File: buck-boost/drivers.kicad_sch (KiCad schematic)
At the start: 30 parts, among them Q7 Q_NPN_BEC, Q8 Q_NPN_BEC, Q9 Q_NPN_BEC, U4 TBA1-1212E, U5 TBA1-1212E

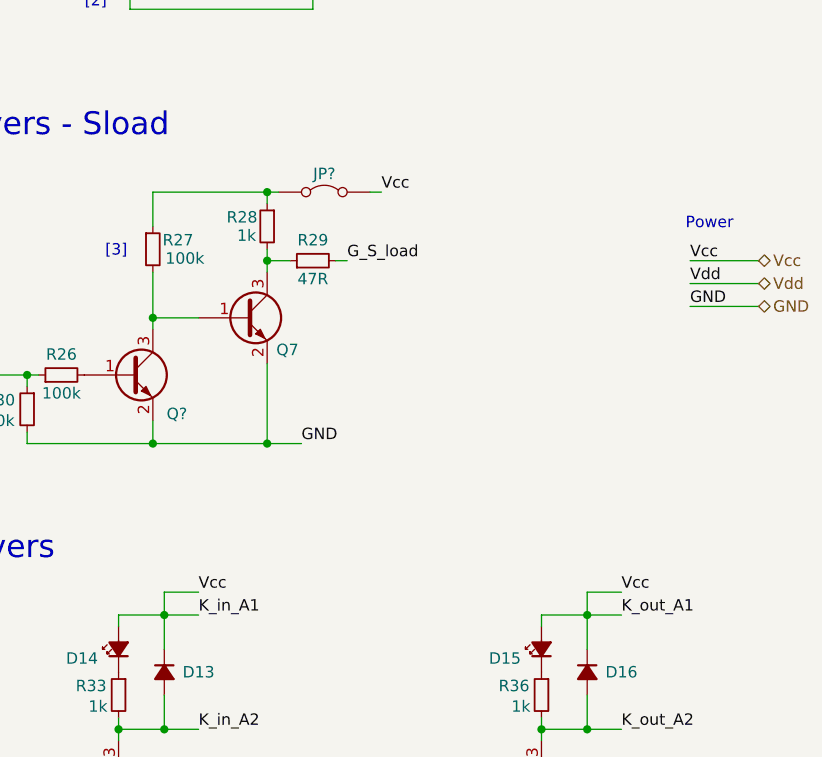
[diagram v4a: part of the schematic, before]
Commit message: The changes indicated in the text document Review. 05.11.2024 were implemented. Missing footprints were added
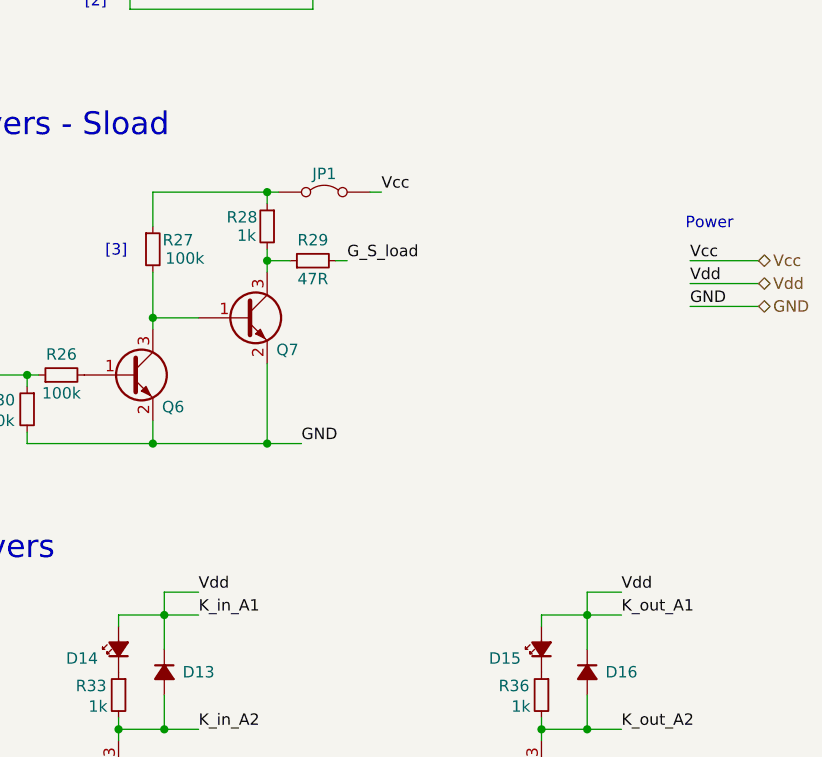
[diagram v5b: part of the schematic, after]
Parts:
- removed Q?: Q_NPN_BEC, Package_TO_SOT_SMD:SOT-23W_Handsoldering, symbol Device:Q_NPN_BEC
- added Q6: Q_NPN_BEC, Package_TO_SOT_SMD:SOT-23W_Handsoldering, symbol Device:Q_NPN_BEC
- D14, D15: footprint (none) -> LED_SMD:LED_0805_2012Metric_Pad1.15x1.40mm_HandSolder
- L2, L4: footprint (none) -> Inductor_SMD:L_0805_2012Metric_Pad1.15x1.40mm_HandSolder
- gave numbers to parts that had none: 1
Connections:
- net GND: now also Q6.2 (E)
- net K_in_A1: no longer C24.1, C27.1, JP1.2 (B), L2.1, L4.1
- net at R26.2: now also Q6.1 (B)
- net at Q7.1 (B), R27.2: now also Q6.3 (C)
- new net Vcc: C24.1, C27.1, JP1.2 (B), L2.1, L4.1
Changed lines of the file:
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@@
+		)
+	)
+	(label "Vdd"
+		(at 54.61 158.75 0)
+		(fields_autoplaced yes)
+		(effects
+			(font
+				(size 1.27 1.27)
+			)
+			(justify left bottom)
 		)
 	)
@@
 	)
 	(label "Vcc"
-		(at 101.6 158.75 0)
-		(fields_autoplaced yes)
-		(effects
-			(font
-				(size 1.27 1.27)
-			)
-			(justify left bottom)
-		)
-	)
-	(label "Vcc"
 		(at 111.76 34.29 180)
 		(fields_autoplaced yes)
@@
 		)
 	)
-	(label "Vcc"
-		(at 54.61 158.75 0)
-		(fields_autoplaced yes)
-		(effects
-			(font
-				(size 1.27 1.27)
-			)
-			(justify left bottom)
-		)
-	)
 	(label "Vcc_S3"
 		(at 160.02 54.61 0)
@@
 	(label "K_out_A1"
 		(at 101.6 161.29 0)
+		(fields_autoplaced yes)
+		(effects
+			(font
+				(size 1.27 1.27)
+			)
+			(justify left bottom)
+		)
+	)
+	(label "Vdd"
+		(at 101.6 158.75 0)
 		(fields_autoplaced yes)
 		(effects
@@
 			)
 		)
-		(property "Footprint" ""
+		(property "Footprint" "Inductor_SMD:L_0805_2012Metric_Pad1.15x1.40mm_HandSolder"
 			(at 124.46 34.29 0)
 			(effects
@@
 			)
 		)
-		(property "Footprint" ""
+		(property "Footprint" "LED_SMD:LED_0805_2012Metric_Pad1.15x1.40mm_HandSolder"
 			(at 45.72 165.1 90)
 			(effects
@@
 		(on_board yes)
 		(dnp no)
-		(property "Reference" "JP?"
+		(property "Reference" "JP1"
 			(at 68.58 112.268 0)
 			(effects
@@
 			(project "buck-boost-xp"
 				(path "/3f994017-d36f-4c43-a8c8-740bd919e8ad/fdca222d-0f97-4e31-8037-fff4f850ee1b"
-					(reference "JP?")
+					(reference "JP1")
 					(unit 1)
 				)
@@
 			)
 		)
-		(property "Footprint" ""
+		(property "Footprint" "LED_SMD:LED_0805_2012Metric_Pad1.15x1.40mm_HandSolder"
 			(at 92.71 165.1 90)
 			(effects
@@
 				(path "/3f994017-d36f-4c43-a8c8-740bd919e8ad/fdca222d-0f97-4e31-8037-fff4f850ee1b"
 					(reference "D15")
-					(unit 1)
-				)
-			)
-		)
-	)
-	(symbol
-		(lib_id "Device:Q_NPN_BEC")
-		(at 46.99 134.62 0)
-		(unit 1)
-		(exclude_from_sim no)
-		(in_bom yes)
-		(on_board yes)
-		(dnp no)
-		(property "Reference" "Q?"
-			(at 51.054 138.938 0)
-			(effects
-				(font
-					(size 1.27 1.27)
-				)
-				(justify left)
-			)
-		)
-		(property "Value" "Q_NPN_BEC"
-			(at 52.07 135.8899 0)
-			(effects
-				(font
-					(size 1.27 1.27)
-				)
-				(justify left)
-				(hide yes)
-			)
-		)
-		(property "Footprint" "Package_TO_SOT_SMD:SOT-23W_Handsoldering"
-			(at 52.07 132.08 0)
-			(effects
-				(font
-					(size 1.27 1.27)
-				)
-				(hide yes)
-			)
-		)
-		(property "Datasheet" "~"
-			(at 46.99 134.62 0)
-			(effects
-				(font
-					(size 1.27 1.27)
-				)
-				(hide yes)
-			)
-		)
-		(property "Description" "NPN transistor, base/emitter/collector"
-			(at 46.99 134.62 0)
-			(effects
-				(font
-					(size 1.27 1.27)
-				)
-				(hide yes)
-			)
-		)
-		(pin "2"
-		)
-		(pin "1"
-		)
-		(pin "3"
-		)
-		(instances
-			(project "buck-boost-xp"
-				(path "/3f994017-d36f-4c43-a8c8-740bd919e8ad/fdca222d-0f97-4e31-8037-fff4f850ee1b"
-					(reference "Q?")
 					(unit 1)
 				)
@@
 			)
 		)
-		(property "Footprint" ""
+		(property "Footprint" "Inductor_SMD:L_0805_2012Metric_Pad1.15x1.40mm_HandSolder"
 			(at 33.02 34.29 0)
 			(effects
@@
 					(unit 1)
 				)
+			)
+		)
+	)
+	(symbol
+		(lib_id "Device:Q_NPN_BEC")
+		(at 46.99 134.62 0)
+		(unit 1)
+		(exclude_from_sim no)
+		(in_bom yes)
+		(on_board yes)
+		(dnp no)
+		(property "Reference" "Q6"
+			(at 50.546 138.176 0)
+			(effects
+				(font
+					(size 1.27 1.27)
+				)
+				(justify left)
+			)
+		)
+		(property "Value" "Q_NPN_BEC"
+			(at 52.07 135.8899 0)
+			(effects
+				(font
+					(size 1.27 1.27)
+				)
+				(justify left)
+				(hide yes)
+			)
+		)
+		(property "Footprint" "Package_TO_SOT_SMD:SOT-23W_Handsoldering"
+			(at 52.07 132.08 0)
+			(effects
+				(font
+					(size 1.27 1.27)
+				)
+				(hide yes)
+			)
+		)
+		(property "Datasheet" "~"
+			(at 46.99 134.62 0)
+			(effects
+				(font
+					(size 1.27 1.27)
+				)
+				(hide yes)
+			)
+		)
+		(property "Description" "NPN transistor, base/emitter/collector"
+			(at 46.99 134.62 0)
+			(effects
+				(font
+					(size 1.27 1.27)
+				)
+				(hide yes)
+			)
+		)
+		(pin "2"
+		)
+		(pin "1"
+		)
+		(pin "3"
+		)
+		(instances
+			(project "buck-boost-xp"
+				(path "/3f994017-d36f-4c43-a8c8-740bd919e8ad/fdca222d-0f97-4e31-8037-fff4f850ee1b"
+					(reference "Q6")
+					(unit 1)
+				)
